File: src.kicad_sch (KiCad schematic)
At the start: 6 parts, among them J1 VCC_5V_9V_DC, J2 Conn_01x19, J3 Conn_01x19, U1 DEVKIT_V1_ESP32-WROOM-32

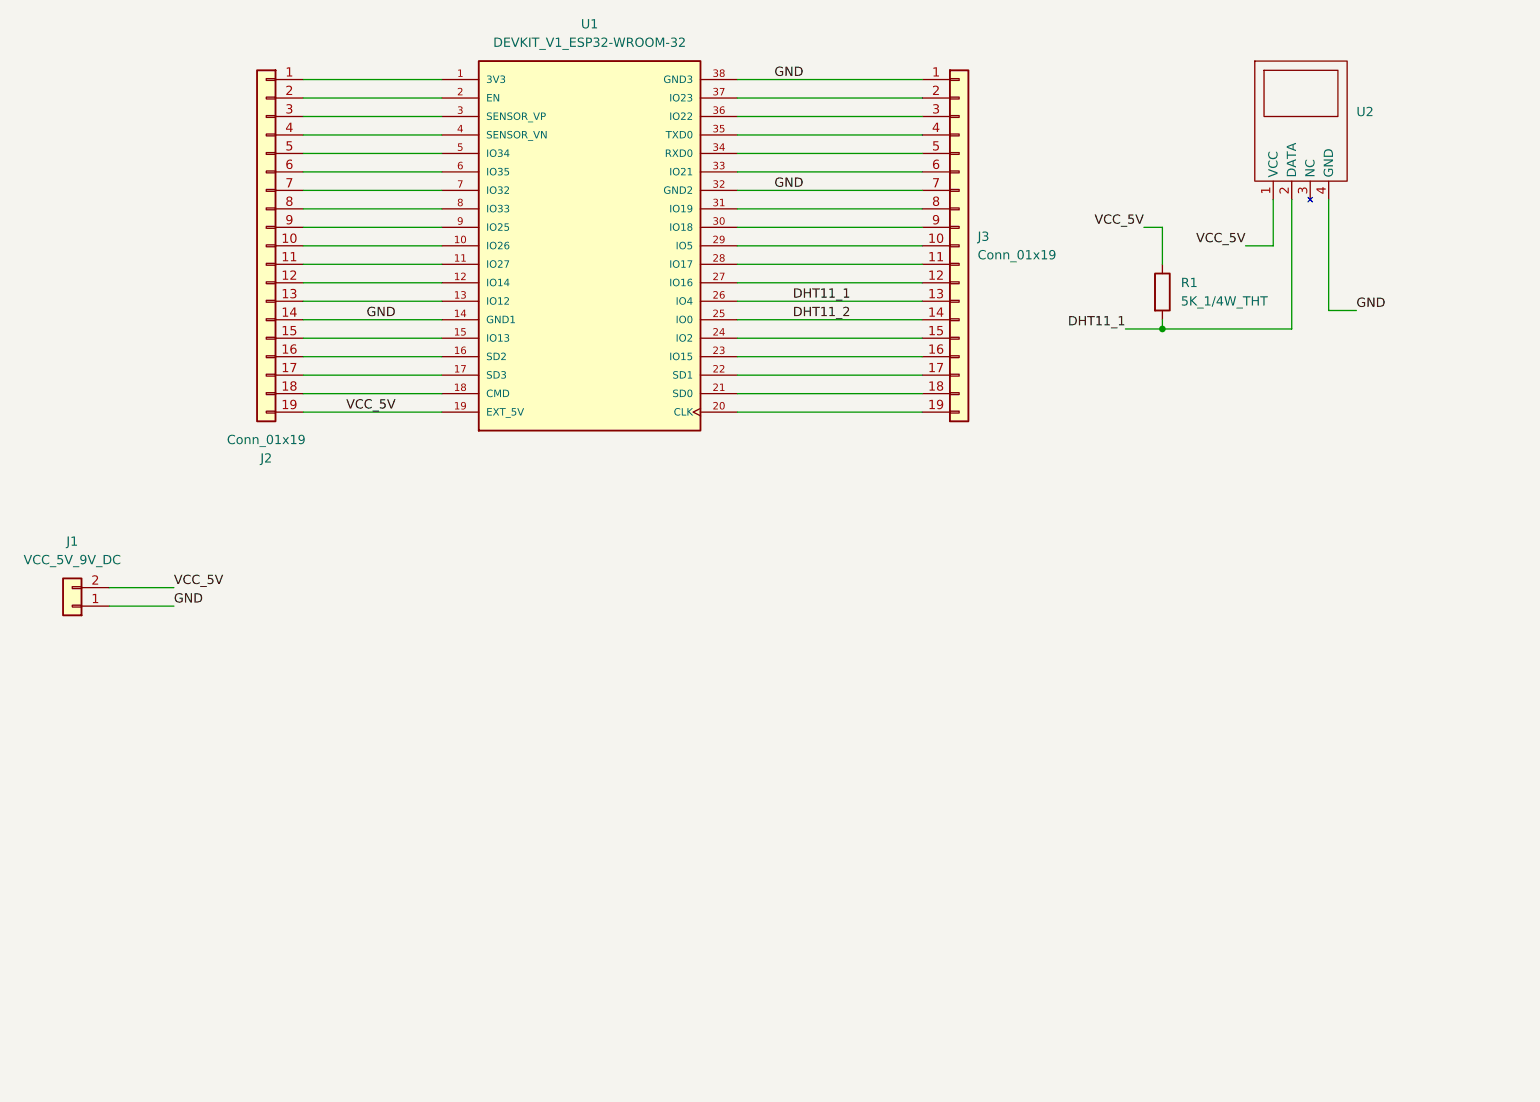
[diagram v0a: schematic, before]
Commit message: added dimensions
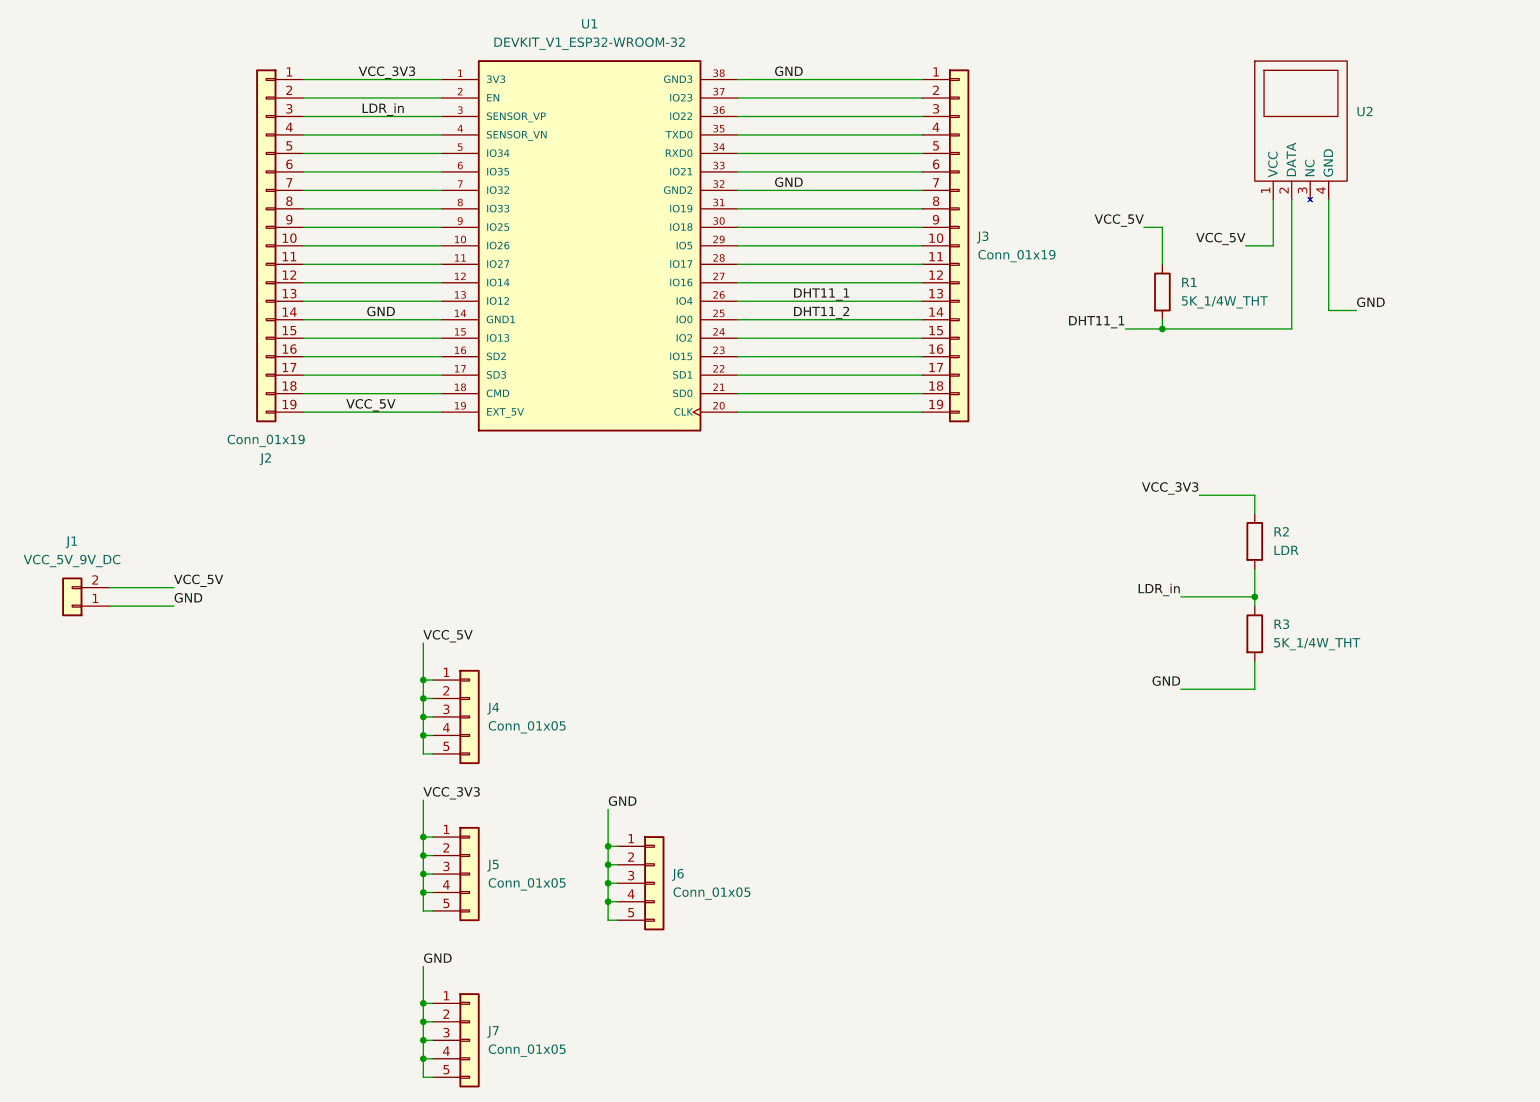
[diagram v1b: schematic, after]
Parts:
- added J4, J5, J6, J7: Conn_01x05, Connector_PinSocket_2.54mm:PinSocket_1x05_P2.54mm_Vertical, symbol Connector_Generic:Conn_01x05
- added R2: LDR, OptoDevice:R_LDR_5.0x4.1mm_P3mm_Vertical, symbol Device:R
- added R3: 5K_1/4W_THT, Resistor_THT:R_Axial_DIN0207_L6.3mm_D2.5mm_P7.62mm_Horizontal, symbol Device:R
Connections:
- net GND: now also J6.1 (Pin_1), J6.2 (Pin_2), J6.3 (Pin_3), J6.4 (Pin_4), J6.5 (Pin_5), J7.1 (Pin_1), J7.2 (Pin_2), J7.3 (Pin_3), J7.4 (Pin_4), J7.5 (Pin_5), R3.2
- net VCC_5V: now also J4.1 (Pin_1), J4.2 (Pin_2), J4.3 (Pin_3), J4.4 (Pin_4), J4.5 (Pin_5)
- net VCC_3V3: now reaches J2.1 (Pin_1), U1.1 (3V3)
- net VCC_3V3: now also J5.1 (Pin_1), J5.2 (Pin_2), J5.3 (Pin_3), J5.4 (Pin_4), J5.5 (Pin_5), R2.1
- net LDR_in: now reaches J2.3 (Pin_3), U1.3 (SENSOR_VP)
- net LDR_in: now also R2.2, R3.1

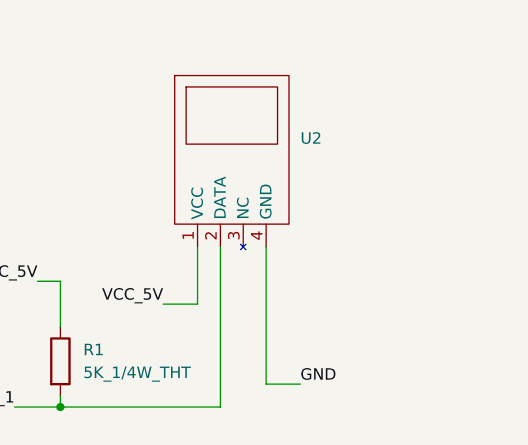
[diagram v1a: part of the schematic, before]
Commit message: added commnets on pcb with perifferals
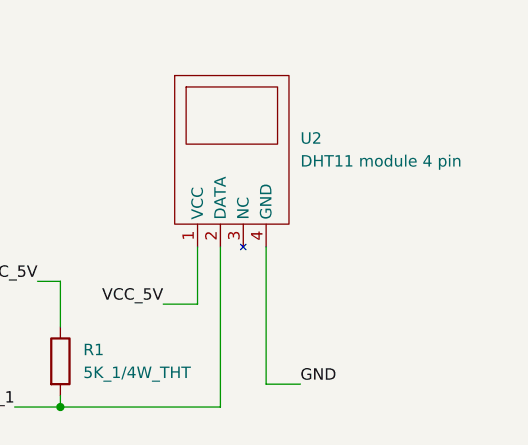
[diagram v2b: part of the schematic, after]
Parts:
- U2: value ~ -> DHT11 module 4 pin

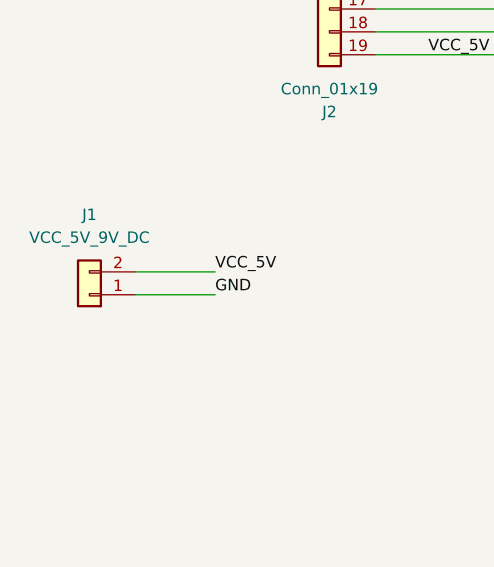
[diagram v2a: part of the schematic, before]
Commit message: increased clearance for pcb manufacturing
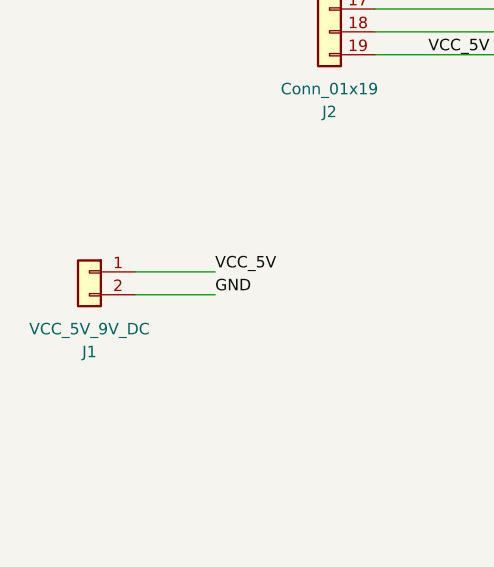
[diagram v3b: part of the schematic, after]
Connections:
- net GND: now also J1.2 (Pin_2); no longer J1.1 (Pin_1)
- net VCC_5V: now also J1.1 (Pin_1); no longer J1.2 (Pin_2)
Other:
- moved on the sheet: J1
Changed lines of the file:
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@@
 	(symbol
 		(lib_id "Connector_Generic:Conn_01x02")
-		(at 26.67 107.95 180)
+		(at 26.67 105.41 0)
+		(mirror y)
 		(unit 1)
 		(exclude_from_sim no)
@@
 		(on_board yes)
 		(dnp no)
-		(fields_autoplaced yes)
 		(property "Reference" "J1"
-			(at 26.67 99.06 0)
+			(at 26.67 114.3 0)
 			(effects
 				(font
@@
 		)
 		(property "Value" "VCC_5V_9V_DC"
-			(at 26.67 101.6 0)
+			(at 26.67 111.76 0)
 			(effects
 				(font
@@
 		)
 		(property "Footprint" "Connector_JST:JST_XH_S2B-XH-A_1x02_P2.50mm_Horizontal"
-			(at 26.67 107.95 0)
+			(at 26.67 105.41 0)
 			(effects
 				(font
@@
 		)
 		(property "Datasheet" "~"
-			(at 26.67 107.95 0)
+			(at 26.67 105.41 0)
 			(effects
 				(font
@@
 		)
 		(property "Description" "Generic connector, single row, 01x02, script generated (kicad-library-utils/schlib/autogen/connector/)"
-			(at 26.67 107.95 0)
+			(at 26.67 105.41 0)
 			(effects
 				(font
@@
 		)
 		(property "Remarks" ""
-			(at 26.67 107.95 0)
+			(at 26.67 105.41 0)
 			(effects
 				(font
@@
 		)
 		(property "Sim.Device" ""
-			(at 26.67 107.95 0)
+			(at 26.67 105.41 0)
 			(effects
 				(font
@@
 		)
 		(property "Sim.Library" ""
-			(at 26.67 107.95 0)
+			(at 26.67 105.41 0)
 			(effects
 				(font
@@
 		)
 		(property "Sim.Name" ""
-			(at 26.67 107.95 0)
+			(at 26.67 105.41 0)
 			(effects
 				(font
@@
 		)
 		(property "Sim.Params" ""
-			(at 26.67 107.95 0)
+			(at 26.67 105.41 0)
 			(effects
 				(font
@@
 		)
 		(property "Sim.Pins" ""
-			(at 26.67 107.95 0)
+			(at 26.67 105.41 0)
 			(effects
 				(font
@@
 		)
 		(property "Vendor" ""
-			(at 26.67 107.95 0)
+			(at 26.67 105.41 0)
 			(effects
 				(font
@@
 		)
 		(property "rotation" ""
-			(at 26.67 107.95 0)
+			(at 26.67 105.41 0)
 			(effects
 				(font
@@
 		)
 		(property "side" ""
-			(at 26.67 107.95 0)
+			(at 26.67 105.41 0)
 			(effects
 				(font
@@
 		)
 		(property "x" ""
-			(at 26.67 107.95 0)
+			(at 26.67 105.41 0)
 			(effects
 				(font
@@
 		)
 		(property "y" ""
-			(at 26.67 107.95 0)
+			(at 26.67 105.41 0)
 			(effects
 				(font
